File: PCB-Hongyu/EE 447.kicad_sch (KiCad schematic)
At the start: 9 parts, among them J1 Conn_01x04_Pin, U2 TSC2046IPWR

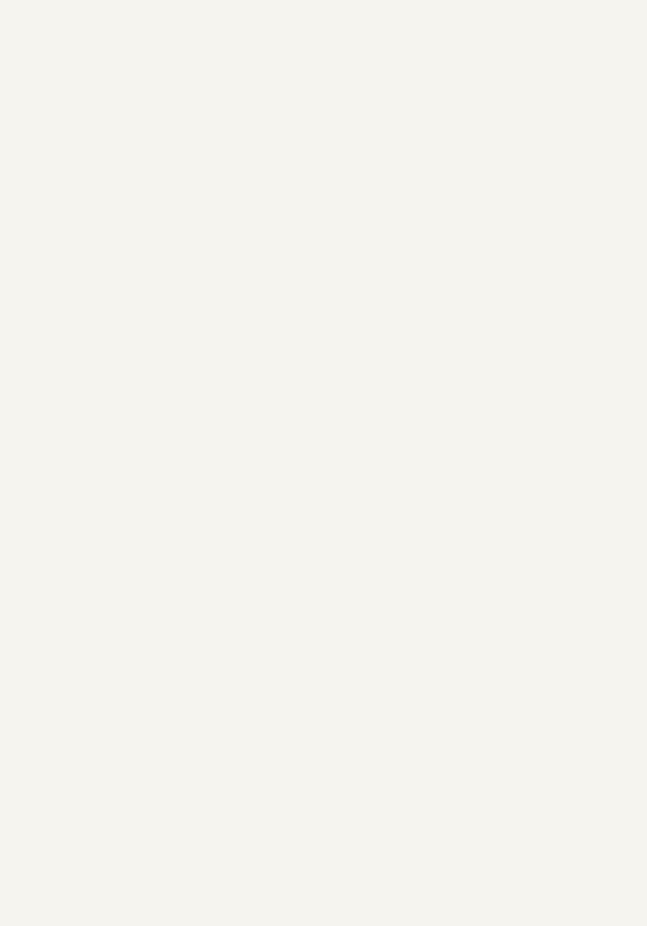
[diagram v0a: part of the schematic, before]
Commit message: added all schematics together
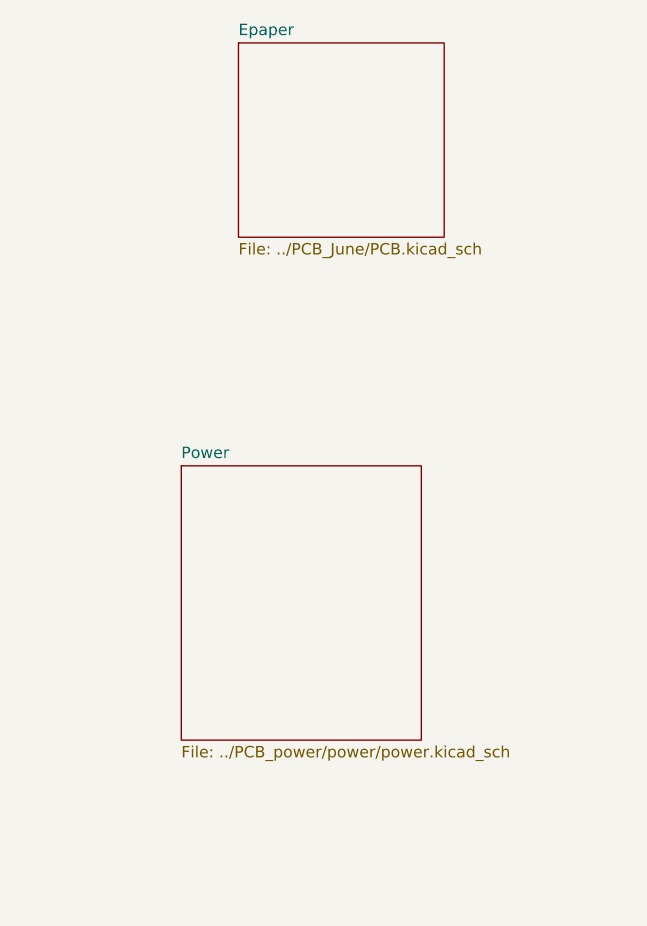
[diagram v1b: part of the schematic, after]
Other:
- added sheet Epaper (../PCB_June/PCB.kicad_sch)
- added sheet Power (../PCB_power/power/power.kicad_sch)
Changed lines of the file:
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@@
 (kicad_sch
-	(version 20231120)
+	(version 20250114)
 	(generator "eeschema")
-	(generator_version "8.0")
+	(generator_version "9.0")
 	(paper "A4")
 	(junction
@@
 		)
 	)
+	(sheet
+		(at 245.11 67.31)
+		(size 26.67 30.48)
+		(exclude_from_sim no)
+		(in_bom yes)
+		(on_board yes)
+		(dnp no)
+		(fields_autoplaced yes)
+		(stroke
+			(width 0.1524)
+			(type solid)
+		)
+		(fill
+			(color 0 0 0 0.0000)
+		)
+		(property "Sheetname" "Power"
+			(at 245.11 66.5984 0)
+			(effects
+				(font
+					(size 1.27 1.27)
+				)
+				(justify left bottom)
+			)
+		)
+		(property "Sheetfile" "../PCB_power/power/power.kicad_sch"
+			(at 245.11 98.3746 0)
+			(effects
+				(font
+					(size 1.27 1.27)
+				)
+				(justify left top)
+			)
+		)
+		(instances
+			(project "EE 447"
+				(path "/8dcae476-bf02-4dea-8567-670805b7ab7c"
+					(page "3")
+				)
+			)
+		)
+	)
+	(sheet
+		(at 251.46 20.32)
+		(size 22.86 21.59)
+		(exclude_from_sim no)
+		(in_bom yes)
+		(on_board yes)
+		(dnp no)
+		(fields_autoplaced yes)
+		(stroke
+			(width 0.1524)
+			(type solid)
+		)
+		(fill
+			(color 0 0 0 0.0000)
+		)
+		(property "Sheetname" "Epaper"
+			(at 251.46 19.6084 0)
+			(effects
+				(font
+					(size 1.27 1.27)
+				)
+				(justify left bottom)
+			)
+		)
+		(property "Sheetfile" "../PCB_June/PCB.kicad_sch"
+			(at 251.46 42.4946 0)
+			(effects
+				(font
+					(size 1.27 1.27)
+				)
+				(justify left top)
+			)
+		)
+		(instances
+			(project "EE 447"
+				(path "/8dcae476-bf02-4dea-8567-670805b7ab7c"
+					(page "2")
+				)
+			)
+		)
+	)
 	(sheet_instances
 		(path "/"
@@
 		)
 	)
+	(embedded_fonts no)
 )

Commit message: started layout placement
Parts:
- renumbered C3 to C1, C4 to C2, C5 to C3, C2 to C4, C6 to C5, C1 to C6, U2 to U1, U1 to U2
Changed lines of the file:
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@@
 		(dnp no)
 		(fields_autoplaced yes)
-		(property "Reference" "U1"
+		(property "Reference" "U2"
 			(at 142.875 48.26 0)
 			(effects
@@
 			(project ""
 				(path "/8dcae476-bf02-4dea-8567-670805b7ab7c"
-					(reference "U1")
+					(reference "U2")
 					(unit 1)
 				)
@@
 		(dnp no)
 		(fields_autoplaced yes)
-		(property "Reference" "#PWR07"
+		(property "Reference" "#PWR03"
 			(at 77.47 138.43 0)
 			(effects
@@
 			(project "EE 447"
 				(path "/8dcae476-bf02-4dea-8567-670805b7ab7c"
-					(reference "#PWR07")
+					(reference "#PWR03")
 					(unit 1)
 				)
@@
 		(dnp no)
 		(fields_autoplaced yes)
-		(property "Reference" "C2"
+		(property "Reference" "C4"
 			(at 83.82 87.6299 0)
 			(effects
@@
 			(project "EE 447"
 				(path "/8dcae476-bf02-4dea-8567-670805b7ab7c"
-					(reference "C2")
+					(reference "C4")
 					(unit 1)
 				)
@@
 		(dnp no)
 		(fields_autoplaced yes)
-		(property "Reference" "#PWR03"
+		(property "Reference" "#PWR06"
 			(at 93.98 100.33 0)
 			(effects
@@
 			(project "EE 447"
 				(path "/8dcae476-bf02-4dea-8567-670805b7ab7c"
-					(reference "#PWR03")
+					(reference "#PWR06")
 					(unit 1)
 				)
@@
 		(dnp no)
 		(fields_autoplaced yes)
-		(property "Reference" "C4"
+		(property "Reference" "C2"
 			(at 68.58 122.5549 0)
 			(effects
@@
 			(project "EE 447"
 				(path "/8dcae476-bf02-4dea-8567-670805b7ab7c"
-					(reference "C4")
+					(reference "C2")
 					(unit 1)
 				)
@@
 		(dnp no)
 		(fields_autoplaced yes)
-		(property "Reference" "#PWR08"
+		(property "Reference" "#PWR05"
 			(at 90.17 138.43 0)
 			(effects
@@
 			(project "EE 447"
 				(path "/8dcae476-bf02-4dea-8567-670805b7ab7c"
-					(reference "#PWR08")
+					(reference "#PWR05")
 					(unit 1)
 				)
@@
 		(dnp no)
 		(fields_autoplaced yes)
-		(property "Reference" "C1"
+		(property "Reference" "C6"
 			(at 97.79 87.6299 0)
 			(effects
@@
 			(project ""
 				(path "/8dcae476-bf02-4dea-8567-670805b7ab7c"
-					(reference "C1")
+					(reference "C6")
 					(unit 1)
 				)
@@
 		(dnp no)
 		(fields_autoplaced yes)
-		(property "Reference" "#PWR05"
+		(property "Reference" "#PWR01"
 			(at 52.07 138.43 0)
 			(effects
@@
 			(project "EE 447"
 				(path "/8dcae476-bf02-4dea-8567-670805b7ab7c"
-					(reference "#PWR05")
+					(reference "#PWR01")
 					(unit 1)
 				)
@@
 		(dnp no)
 		(fields_autoplaced yes)
-		(property "Reference" "#PWR06"
+		(property "Reference" "#PWR02"
 			(at 64.77 138.43 0)
 			(effects
@@
 			(project "EE 447"
 				(path "/8dcae476-bf02-4dea-8567-670805b7ab7c"
-					(reference "#PWR06")
+					(reference "#PWR02")
 					(unit 1)
 				)
@@
 		(dnp no)
 		(fields_autoplaced yes)
-		(property "Reference" "#PWR02"
+		(property "Reference" "#PWR08"
 			(at 120.65 69.85 0)
 			(effects
@@
 			(project "EE 447"
 				(path "/8dcae476-bf02-4dea-8567-670805b7ab7c"
-					(reference "#PWR02")
+					(reference "#PWR08")
 					(unit 1)
 				)
@@
 		(dnp no)
 		(fields_autoplaced yes)
-		(property "Reference" "U2"
+		(property "Reference" "U1"
 			(at 143.51 92.71 0)
 			(effects
@@
 			(project ""
 				(path "/8dcae476-bf02-4dea-8567-670805b7ab7c"
-					(reference "U2")
+					(reference "U1")
 					(unit 1)
 				)
@@
 		(dnp no)
 		(fields_autoplaced yes)
-		(property "Reference" "C5"
+		(property "Reference" "C3"
 			(at 81.28 122.5549 0)
 			(effects
@@
 			(project "EE 447"
 				(path "/8dcae476-bf02-4dea-8567-670805b7ab7c"
-					(reference "C5")
+					(reference "C3")
 					(unit 1)
 				)
@@
 		(dnp no)
 		(fields_autoplaced yes)
-		(property "Reference" "C6"
+		(property "Reference" "C5"
 			(at 93.98 122.5549 0)
 			(effects
@@
 			(project "EE 447"
 				(path "/8dcae476-bf02-4dea-8567-670805b7ab7c"
-					(reference "C6")
+					(reference "C5")
 					(unit 1)
 				)
@@
 		(dnp no)
 		(fields_autoplaced yes)
-		(property "Reference" "#PWR01"
+		(property "Reference" "#PWR07"
 			(at 101.6 127 0)
 			(effects
@@
 			(project ""
 				(path "/8dcae476-bf02-4dea-8567-670805b7ab7c"
-					(reference "#PWR01")
+					(reference "#PWR07")
 					(unit 1)
 				)
@@
 		(dnp no)
 		(fields_autoplaced yes)
-		(property "Reference" "C3"
+		(property "Reference" "C1"
 			(at 55.88 122.5549 0)
 			(effects
@@
 			(project "EE 447"
 				(path "/8dcae476-bf02-4dea-8567-670805b7ab7c"
-					(reference "C3")
+					(reference "C1")
 					(unit 1)
 				)
@@
 	)
 	(sheet
-		(at 251.46 20.32)
-		(size 22.86 21.59)
+		(at 203.2 26.67)
+		(size 22.86 29.21)
 		(exclude_from_sim no)
 		(in_bom yes)
@@
 		)
 		(property "Sheetname" "Epaper"
-			(at 251.46 19.6084 0)
+			(at 203.2 25.9584 0)
 			(effects
 				(font
@@
 		)
 		(property "Sheetfile" "../PCB_June/PCB.kicad_sch"
-			(at 251.46 42.4946 0)
+			(at 203.2 56.4646 0)
 			(effects
 				(font
@@
 			(project "EE 447"
 				(path "/8dcae476-bf02-4dea-8567-670805b7ab7c"
-					(page "2")
-				)
-			)
+					(page "3")
+				)
+			)

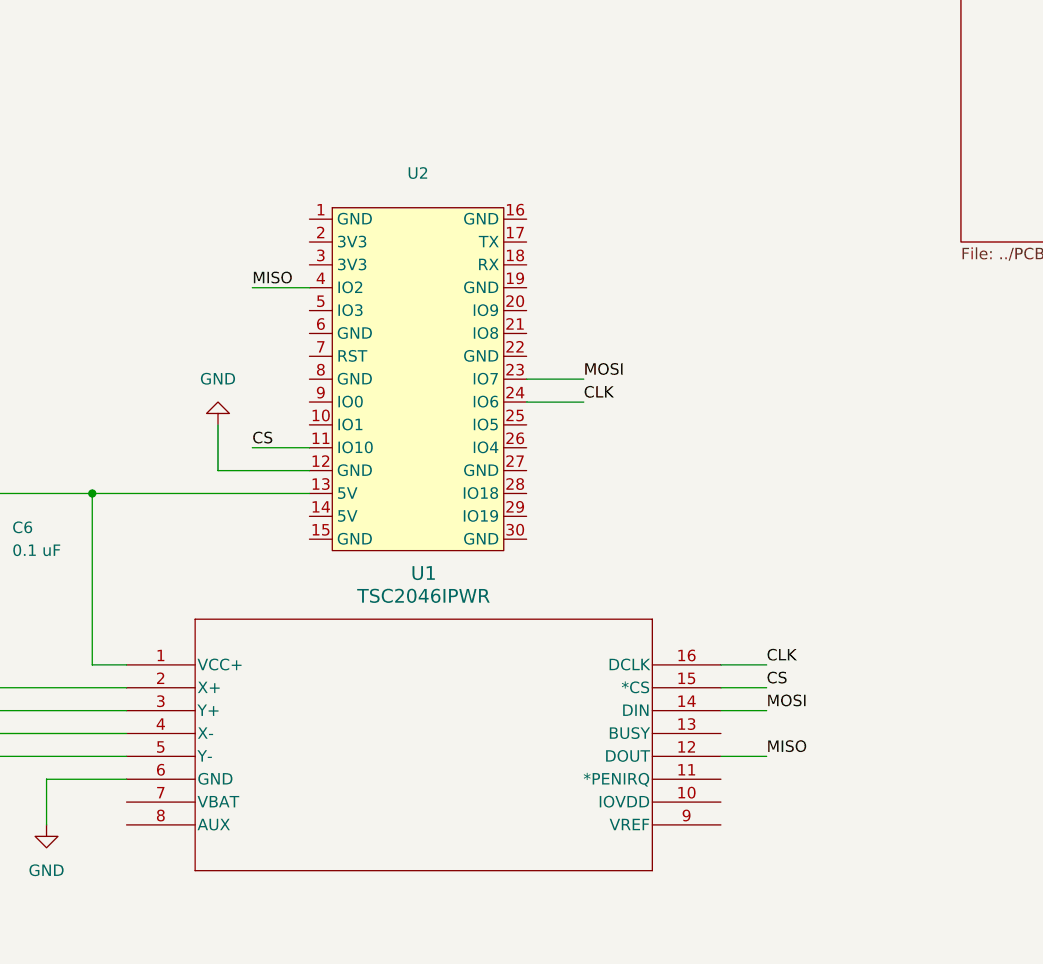
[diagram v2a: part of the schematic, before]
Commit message: spi global pins
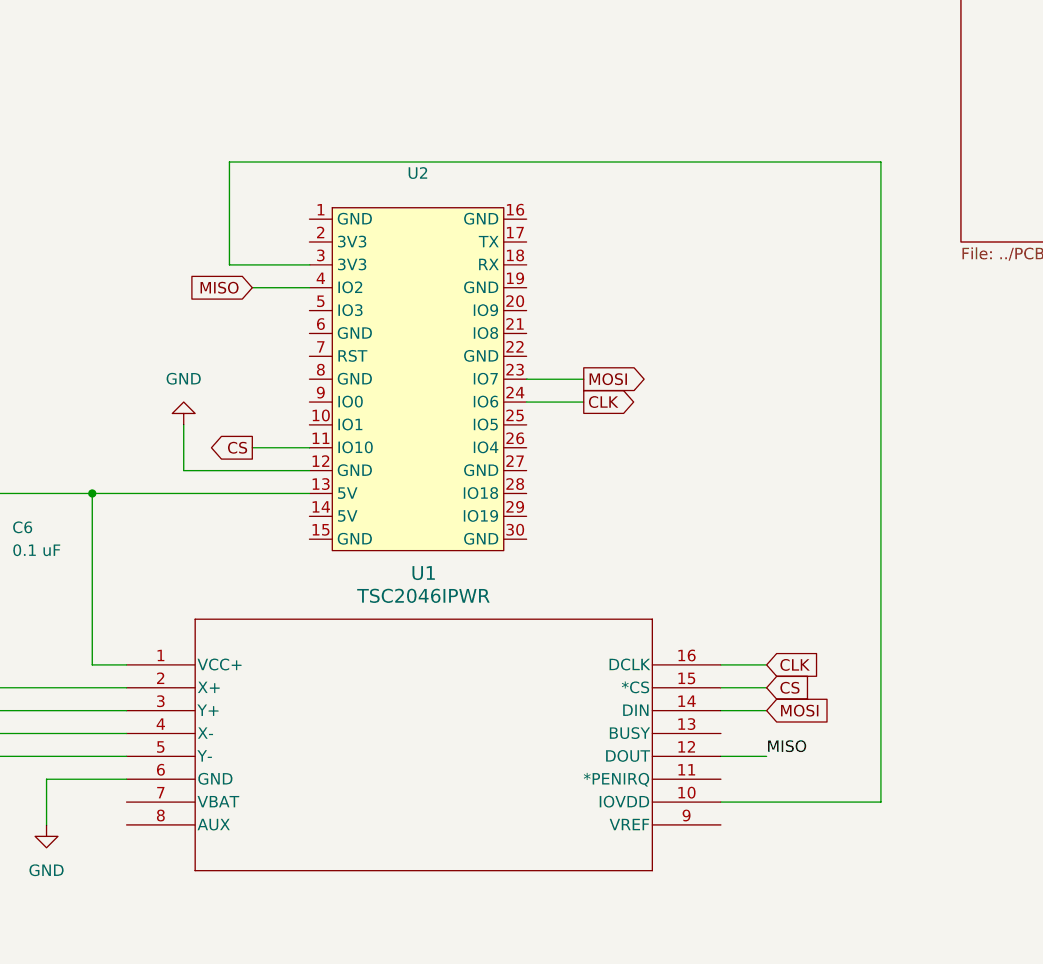
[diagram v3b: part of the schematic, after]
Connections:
- net at U2.3 (3V3): now also U1.10 (IOVDD)
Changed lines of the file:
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@@
+	(wire
+		(pts
+			(xy 121.92 58.42) (xy 130.81 58.42)
+		)
+		(stroke
+			(width 0)
+			(type default)
+		)
+	)
 	(wire
 		(pts
@@
 	(wire
 		(pts
-			(xy 120.65 76.2) (xy 120.65 81.28)
+			(xy 116.84 76.2) (xy 116.84 81.28)
 		)
 		(stroke
@@
 	(wire
 		(pts
+			(xy 176.53 118.11) (xy 194.31 118.11)
+		)
+		(stroke
+			(width 0)
+			(type default)
+		)
+	)
+	(wire
+		(pts
 			(xy 44.45 105.41) (xy 52.07 105.41)
 		)
@@
 	(wire
 		(pts
+			(xy 194.31 46.99) (xy 121.92 46.99)
+		)
+		(stroke
+			(width 0)
+			(type default)
+		)
+	)
+	(wire
+		(pts
 			(xy 110.49 115.57) (xy 101.6 115.57)
 		)
@@
 	(wire
 		(pts
-			(xy 120.65 81.28) (xy 130.81 81.28)
+			(xy 116.84 81.28) (xy 130.81 81.28)
 		)
 		(stroke
@@
 	(wire
 		(pts
+			(xy 194.31 118.11) (xy 194.31 46.99)
+		)
+		(stroke
+			(width 0)
+			(type default)
+		)
+	)
+	(wire
+		(pts
 			(xy 93.98 92.71) (xy 93.98 93.98)
 		)
@@
 	(wire
 		(pts
+			(xy 121.92 46.99) (xy 121.92 58.42)
+		)
+		(stroke
+			(width 0)
+			(type default)
+		)
+	)
+	(wire
+		(pts
 			(xy 77.47 127) (xy 77.47 132.08)
 		)
@@
 			(width 0)
 			(type default)
-		)
-	)
-	(label "MOSI"
-		(at 161.29 71.12 0)
-		(effects
-			(font
-				(size 1.27 1.27)
-			)
-			(justify left bottom)
-		)
-	)
-	(label "CS"
-		(at 181.61 105.41 0)
-		(effects
-			(font
-				(size 1.27 1.27)
-			)
-			(justify left bottom)
-		)
-	)
-	(label "CLK"
-		(at 181.61 102.87 0)
-		(effects
-			(font
-				(size 1.27 1.27)
-			)
-			(justify left bottom)
 		)
 	)
@@
 		)
 	)
-	(label "CS"
-		(at 124.46 78.74 0)
+	(global_label "CLK"
+		(shape input)
+		(at 181.61 102.87 0)
+		(fields_autoplaced yes)
 		(effects
 			(font
 				(size 1.27 1.27)
 			)
-			(justify left bottom)
-		)
-	)
-	(label "CLK"
-		(at 161.29 73.66 0)
+			(justify left)
+		)
+		(property "Intersheetrefs" "${INTERSHEET_REFS}"
+			(at 188.1633 102.87 0)
+			(effects
+				(font
+					(size 1.27 1.27)
+				)
+				(justify left)
+				(hide yes)
+			)
+		)
+	)
+	(global_label "CS"
+		(shape input)
+		(at 181.61 105.41 0)
+		(fields_autoplaced yes)
 		(effects
 			(font
 				(size 1.27 1.27)
 			)
-			(justify left bottom)
-		)
-	)
-	(label "MOSI"
-		(at 181.61 107.95 0)
+			(justify left)
+		)
+		(property "Intersheetrefs" "${INTERSHEET_REFS}"
+			(at 187.0747 105.41 0)
+			(effects
+				(font
+					(size 1.27 1.27)
+				)
+				(justify left)
+				(hide yes)
+			)
+		)
+	)
+	(global_label "MISO"
+		(shape input)
+		(at 124.46 60.96 180)
+		(fields_autoplaced yes)
 		(effects
 			(font
 				(size 1.27 1.27)
 			)
-			(justify left bottom)
-		)
-	)
-	(label "MISO"
-		(at 124.46 60.96 0)
+			(justify right)
+		)
+		(property "Intersheetrefs" "${INTERSHEET_REFS}"
+			(at 116.8786 60.96 0)
+			(effects
+				(font
+					(size 1.27 1.27)
+				)
+				(justify right)
+				(hide yes)
+			)
+		)
+	)
+	(global_label "MOSI"
+		(shape output)
+		(at 161.29 71.12 0)
+		(fields_autoplaced yes)
 		(effects
 			(font
 				(size 1.27 1.27)
 			)
-			(justify left bottom)
+			(justify left)
+		)
+		(property "Intersheetrefs" "${INTERSHEET_REFS}"
+			(at 168.8714 71.12 0)
+			(effects
+				(font
+					(size 1.27 1.27)
+				)
+				(justify left)
+				(hide yes)
+			)
+		)
+	)
+	(global_label "CLK"
+		(shape output)
+		(at 161.29 73.66 0)
+		(fields_autoplaced yes)
+		(effects
+			(font
+				(size 1.27 1.27)
+			)
+			(justify left)
+		)
+		(property "Intersheetrefs" "${INTERSHEET_REFS}"
+			(at 167.8433 73.66 0)
+			(effects
+				(font
+					(size 1.27 1.27)
+				)
+				(justify left)
+				(hide yes)
+			)
+		)
+	)
+	(global_label "CS"
+		(shape output)
+		(at 124.46 78.74 180)
+		(fields_autoplaced yes)
+		(effects
+			(font
+				(size 1.27 1.27)
+			)
+			(justify right)
+		)
+		(property "Intersheetrefs" "${INTERSHEET_REFS}"
+			(at 118.9953 78.74 0)
+			(effects
+				(font
+					(size 1.27 1.27)
+				)
+				(justify right)
+				(hide yes)
+			)
+		)
+	)
+	(global_label "MOSI"
+		(shape input)
+		(at 181.61 107.95 0)
+		(fields_autoplaced yes)
+		(effects
+			(font
+				(size 1.27 1.27)
+			)
+			(justify left)
+		)
+		(property "Intersheetrefs" "${INTERSHEET_REFS}"
+			(at 189.1914 107.95 0)
+			(effects
+				(font
+					(size 1.27 1.27)
+				)
+				(justify left)
+				(hide yes)
+			)
 		)
 	)
@@
 	(symbol
 		(lib_id "power:GND")
-		(at 120.65 76.2 180)
+		(at 116.84 76.2 180)
 		(unit 1)
 		(exclude_from_sim no)
@@
 		(fields_autoplaced yes)
 		(property "Reference" "#PWR08"
-			(at 120.65 69.85 0)
+			(at 116.84 69.85 0)
 			(effects
 				(font
@@
 		)
 		(property "Value" "GND"
-			(at 120.65 71.12 0)
+			(at 116.84 71.12 0)
 			(effects
 				(font
@@
 		)
 		(property "Footprint" ""
-			(at 120.65 76.2 0)
+			(at 116.84 76.2 0)
 			(effects
 				(font
@@
 		)
 		(property "Datasheet" ""
-			(at 120.65 76.2 0)
+			(at 116.84 76.2 0)
 			(effects
 				(font
@@
 		)
 		(property "Description" "Power symbol creates a global label with name \"GND\" , ground"
-			(at 120.65 76.2 0)
-			(effects
-				(font
+			(at 116.84 76.2 0)
+			(effects
+				(font

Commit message: power nets
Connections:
- net GND: now also U2.1 (GND), U2.15 (GND), U2.16 (GND), U2.19 (GND), U2.22 (GND), U2.27 (GND), U2.30 (GND), U2.6 (GND), U2.8 (GND)
- net +5V: now reaches C4.1, C6.1, U1.1 (VCC+)
- net +5V: no longer U2.13 (5V)
- net VUSB: now reaches U2.14 (5V)
- net VUSB: now also U2.13 (5V)
- net +3.3V: now reaches U2.2 (3V3)
- net +3.3V: now also U1.10 (IOVDD), U2.3 (3V3)
- net +BATT: now reaches U1.7 (VBAT)
- net CS renamed CS_TSC
- no-connect marks 0 -> 2
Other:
- moved on the sheet: C4, C6
